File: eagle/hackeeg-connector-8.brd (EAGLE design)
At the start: 114.3 x 30.5 mm, 21 parts

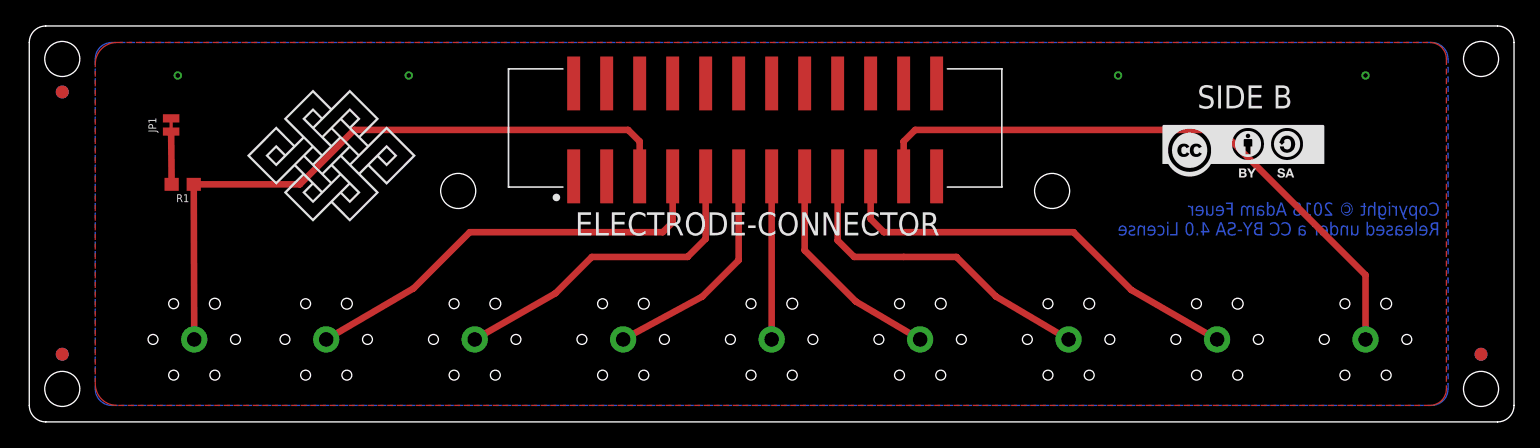
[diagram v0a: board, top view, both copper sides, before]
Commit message: corrected connector spacing and made board smaller
- all connectors are now evenly spaced
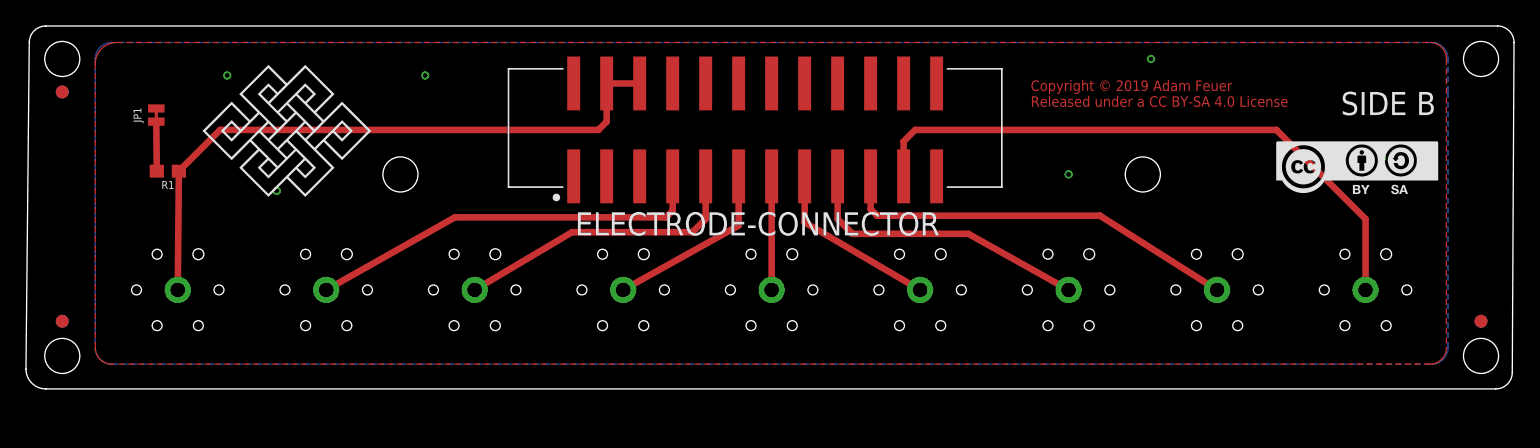
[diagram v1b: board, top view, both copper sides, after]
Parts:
- moved U$13 8.85 mm to (95.9, 17.3)
- moved AGND 4.02 mm to (11.4, 10.2)
- moved U$1 3.92 mm to (19.9, 22.4)
- moved IN1P 3.81 mm to (22.9, 10.2)
- moved IN2P 3.81 mm to (34.3, 10.2)
- moved IN3P 3.81 mm to (45.7, 10.2)
- moved IN4P 3.81 mm to (57.1, 10.2)
- moved IN5P 3.81 mm to (68.6, 10.2)
- moved IN6P 3.81 mm to (80.0, 10.2)
- moved IN7P 3.81 mm to (91.4, 10.2)
- moved IN8P 3.81 mm to (102.9, 10.2)
- moved FD1 2.54 mm to (2.54, 7.75)
- moved FD3 2.54 mm to (111.8, 7.75)
- moved FD4 2.54 mm to (111.8, 7.75)
- moved FD6 2.54 mm to (2.54, 7.75)
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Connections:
- net AGND: no longer ELECTRODE-CONNECTOR.4, ELECTRODE-CONNECTOR.6
- net AGND1: now also ELECTRODE-CONNECTOR.4, ELECTRODE-CONNECTOR.6; no longer ELECTRODE-CONNECTOR.5
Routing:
- net N$5: track 12.6 -> 8.74 mm
- net N$4: track 17.3 -> 14.0 mm
- net N$6: track 17.0 -> 13.8 mm
- net N$7: track 25.4 -> 22.7 mm
- net N$3: track 25.3 -> 22.7 mm
- net N$2: track 33.4 -> 31.0 mm
- net N$8: track 33.2 -> 31.1 mm
- net AGND1: track 51.1 -> 49.1 mm
- net N$9: track 48.2 -> 46.9 mm
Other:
- board size 114.3 x 30.5 mm -> 114.6 x 27.9 mm
- board text added: "Copyright © 2019 Adam Feuer Released under a CC BY-SA 4.0 License"
- board text removed: "Copyright © 2018 Adam Feuer Released under a CC BY-SA 4.0 License"

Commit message: made mounting holes 3.3mm to fit m3 screws
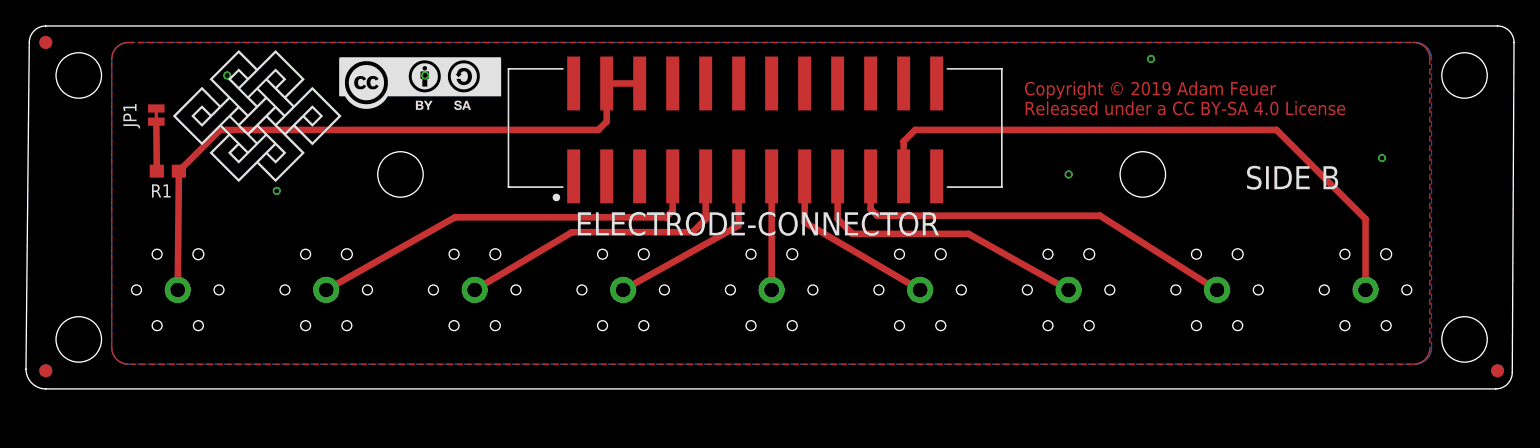
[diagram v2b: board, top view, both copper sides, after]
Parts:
- moved U$13 72.4 mm to (23.7, 23.7)
- moved FD2 4.02 mm to (1.27, 29.2)
- moved FD5 4.02 mm to (1.27, 29.2)
- moved FD1 4.02 mm to (1.27, 3.94)
- moved FD6 4.02 mm to (1.27, 3.94)
- moved FD3 4.02 mm to (113.0, 3.94)
- moved FD4 4.02 mm to (113.0, 3.94)
- moved U$1 2.56 mm to (17.7, 23.5)
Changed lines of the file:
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@@
 <board>
 <plain>
-<text x="77.089" y="24.257" size="0.8128" layer="1">Copyright © 2019 Adam Feuer
+<text x="76.581" y="23.622" size="1.016" layer="1">Copyright © 2019 Adam Feuer
 Released under a CC BY-SA 4.0 License</text>
-<hole x="2.54" y="27.94" drill="2.69999375"/>
-<hole x="2.54" y="5.08" drill="2.69999375"/>
-<hole x="111.76" y="5.08" drill="2.69999375"/>
-<hole x="111.76" y="27.94" drill="2.69999375"/>
+<hole x="3.81" y="26.67" drill="3.49999375"/>
+<hole x="3.81" y="6.35" drill="3.49999375"/>
+<hole x="110.49" y="6.35" drill="3.49999375"/>
+<hole x="110.49" y="26.67" drill="3.49999375"/>
 <dimension x1="0" y1="34.29" x2="114.3" y2="34.29" x3="57.15" y3="40.64" textsize="1.778" layer="47" unit="inch"/>
 <wire x1="1.27" y1="2.54" x2="112.896296875" y2="2.54" width="0" layer="20"/>
@@
 <wire x1="0" y1="29.21" x2="-0.254" y2="4.064" width="0" layer="20"/>
 <wire x1="-0.254" y1="4.064" x2="1.27" y2="2.54" width="0" layer="20" curve="90"/>
-<text x="108.331" y="26.035" size="1.778" layer="26" rot="MR0">SIDE A</text>
-<text x="100.965" y="23.622" size="1.778" layer="25">SIDE B</text>
-<hole x="28.575" y="19.05" drill="2.69999375"/>
-<hole x="85.725" y="19.05" drill="2.69999375"/>
+<text x="100.965" y="20.32" size="1.778" layer="26" rot="MR0">SIDE A</text>
+<text x="93.599" y="17.907" size="1.778" layer="25">SIDE B</text>
+<hole x="28.575" y="19.05" drill="3.49999375"/>
+<hole x="85.725" y="19.05" drill="3.49999375"/>
 <dimension x1="-2.54" y1="30.48" x2="-2.54" y2="2.54" x3="-8.89" y3="16.51" textsize="1.778" layer="47" unit="inch"/>
 </plain>
@@
 <element name="IN6P" library="po-37729" package="HEX-110" value="PO37729HEX-110" x="80.01" y="10.16" rot="MR0"/>
 <element name="IN7P" library="po-37729" package="HEX-110" value="PO37729HEX-110" x="91.44" y="10.16" rot="MR0"/>
-<element name="U$1" library="endless-knot" package="ENDLESSKNOT-MEDIUM" value="ENDLESSKNOTENDLESSKNOT-MEDIUM" x="19.939" y="22.352"/>
-<element name="U$13" library="creative-commons" package="CC-BY-SA" value="CC-BY-SA" x="95.885" y="17.272"/>
+<element name="U$1" library="endless-knot" package="ENDLESSKNOT-MEDIUM" value="ENDLESSKNOTENDLESSKNOT-MEDIUM" x="17.653" y="23.495"/>
+<element name="U$13" library="creative-commons" package="CC-BY-SA" value="CC-BY-SA" x="23.749" y="23.749"/>
 <element name="IN8P" library="po-37729" package="HEX-110" value="PO37729HEX-110" x="102.87" y="10.16" rot="MR0"/>
-<element name="FD1" library="SparkFun-Aesthetics" library_urn="urn:adsk.eagle:library:507" package="FIDUCIAL-1X2" package3d_urn="urn:adsk.eagle:package:37108/1" value="FIDUCIAL1X2" x="2.54" y="7.747"/>
-<element name="FD2" library="SparkFun-Aesthetics" library_urn="urn:adsk.eagle:library:507" package="FIDUCIAL-1X2" package3d_urn="urn:adsk.eagle:package:37108/1" value="FIDUCIAL1X2" x="2.54" y="25.4"/>
-<element name="FD3" library="SparkFun-Aesthetics" library_urn="urn:adsk.eagle:library:507" package="FIDUCIAL-1X2" package3d_urn="urn:adsk.eagle:package:37108/1" value="FIDUCIAL1X2" x="111.76" y="7.747"/>
-<element name="FD4" library="SparkFun-Aesthetics" library_urn="urn:adsk.eagle:library:507" package="FIDUCIAL-1X2" package3d_urn="urn:adsk.eagle:package:37108/1" value="FIDUCIAL1X2" x="111.76" y="7.747" rot="MR0"/>
-<element name="FD5" library="SparkFun-Aesthetics" library_urn="urn:adsk.eagle:library:507" package="FIDUCIAL-1X2" package3d_urn="urn:adsk.eagle:package:37108/1" value="FIDUCIAL1X2" x="2.54" y="25.4" rot="MR0"/>
-<element name="FD6" library="SparkFun-Aesthetics" library_urn="urn:adsk.eagle:library:507" package="FIDUCIAL-1X2" package3d_urn="urn:adsk.eagle:package:37108/1" value="FIDUCIAL1X2" x="2.54" y="7.747" rot="MR0"/>
-<element name="R1" library="SparkFun-Resistors" library_urn="urn:adsk.eagle:library:532" package="0603" package3d_urn="urn:adsk.eagle:package:39650/1" value="0" x="10.668" y="19.304" rot="R180">
+<element name="FD1" library="SparkFun-Aesthetics" library_urn="urn:adsk.eagle:library:507" package="FIDUCIAL-1X2" package3d_urn="urn:adsk.eagle:package:37108/1" value="FIDUCIAL1X2" x="1.27" y="3.937"/>
+<element name="FD2" library="SparkFun-Aesthetics" library_urn="urn:adsk.eagle:library:507" package="FIDUCIAL-1X2" package3d_urn="urn:adsk.eagle:package:37108/1" value="FIDUCIAL1X2" x="1.27" y="29.21"/>
+<element name="FD3" library="SparkFun-Aesthetics" library_urn="urn:adsk.eagle:library:507" package="FIDUCIAL-1X2" package3d_urn="urn:adsk.eagle:package:37108/1" value="FIDUCIAL1X2" x="113.03" y="3.937"/>
+<element name="FD4" library="SparkFun-Aesthetics" library_urn="urn:adsk.eagle:library:507" package="FIDUCIAL-1X2" package3d_urn="urn:adsk.eagle:package:37108/1" value="FIDUCIAL1X2" x="113.03" y="3.937" rot="MR0"/>
+<element name="FD5" library="SparkFun-Aesthetics" library_urn="urn:adsk.eagle:library:507" package="FIDUCIAL-1X2" package3d_urn="urn:adsk.eagle:package:37108/1" value="FIDUCIAL1X2" x="1.27" y="29.21" rot="MR0"/>
+<element name="FD6" library="SparkFun-Aesthetics" library_urn="urn:adsk.eagle:library:507" package="FIDUCIAL-1X2" package3d_urn="urn:adsk.eagle:package:37108/1" value="FIDUCIAL1X2" x="1.27" y="3.937" rot="MR0"/>
+<element name="R1" library="SparkFun-Resistors" library_urn="urn:adsk.eagle:library:532" package="0603" package3d_urn="urn:adsk.eagle:package:39650/1" value="0" x="10.668" y="19.304" smashed="yes" rot="R180">
+<attribute name="NAME" x="10.16" y="18.288" size="1.016" layer="25" font="vector" ratio="20" rot="R180" align="bottom-center"/>
 <attribute name="PROD_ID" value="RES-08609" x="10.668" y="19.304" size="1.778" layer="27" rot="R180" display="off"/>
+<attribute name="VALUE" x="10.668" y="20.066" size="0.6096" layer="27" font="vector" ratio="20" rot="R180" align="top-center"/>
 </element>
-<element name="JP1" library="SparkFun-Jumpers" library_urn="urn:adsk.eagle:library:528" package="SMT-JUMPER_2_NC_TRACE_NO-SILK" package3d_urn="urn:adsk.eagle:package:39286/1" value="JUMPER-SMT_2_NC_TRACE_NO-SILK" x="9.779" y="23.622" rot="R90"/>
+<element name="JP1" library="SparkFun-Jumpers" library_urn="urn:adsk.eagle:library:528" package="SMT-JUMPER_2_NC_TRACE_NO-SILK" package3d_urn="urn:adsk.eagle:package:39286/1" value="JUMPER-SMT_2_NC_TRACE_NO-SILK" x="9.779" y="23.622" smashed="yes" rot="R90">
+<attribute name="NAME" x="8.255" y="23.622" size="1.016" layer="25" font="vector" ratio="20" rot="R90" align="bottom-center"/>
+<attribute name="VALUE" x="10.922" y="23.622" size="0.6096" layer="27" font="vector" ratio="20" rot="R90" align="top-center"/>
+</element>
 </elements>
 <signals>
@@
 <signal name="AGND">
 <polygon width="0.1524" layer="1">
-<vertex x="109.093" y="27.94"/>
-<vertex x="109.093" y="5.715" curve="-90"/>
-<vertex x="107.823" y="4.445"/>
-<vertex x="6.35" y="4.445" curve="-90"/>
-<vertex x="5.08" y="5.715"/>
-<vertex x="5.08" y="27.559" curve="-90"/>
-<vertex x="6.731" y="29.21"/>
-<vertex x="107.823" y="29.21" curve="-90"/>
+<vertex x="6.35" y="5.715"/>
+<vertex x="6.35" y="27.94" curve="-90"/>
+<vertex x="7.62" y="29.21"/>
+<vertex x="106.553" y="29.21" curve="-90"/>
+<vertex x="107.823" y="27.94"/>
+<vertex x="107.823" y="5.715" curve="-90"/>
+<vertex x="106.553" y="4.445"/>
+<vertex x="7.62" y="4.445" curve="-90"/>
 </polygon>
 <contactref element="ELECTRODE-CONNECTOR" pad="8"/>
@@
 <polygon width="0.0762" layer="16">
 <vertex x="8.89" y="29.21"/>
-<vertex x="6.35" y="29.21" curve="90"/>
-<vertex x="5.08" y="27.94"/>
-<vertex x="5.08" y="5.715" curve="90"/>
-<vertex x="6.35" y="4.445"/>
+<vertex x="7.62" y="29.21" curve="90"/>
+<vertex x="6.35" y="27.94"/>
+<vertex x="6.35" y="5.715" curve="90"/>
+<vertex x="7.62" y="4.445"/>
 <vertex x="102.235" y="4.445"/>
-<vertex x="107.95" y="4.445" curve="90"/>
-<vertex x="109.22" y="5.715"/>
-<vertex x="109.22" y="25.4"/>
-<vertex x="109.22" y="27.94" curve="90"/>
-<vertex x="107.95" y="29.21"/>
+<vertex x="106.68" y="4.445" curve="90"/>
+<vertex x="107.95" y="5.715"/>
+<vertex x="107.95" y="24.13"/>
+<vertex x="107.95" y="27.94" curve="90"/>
+<vertex x="106.68" y="29.21"/>
 </polygon>
 </signal>
